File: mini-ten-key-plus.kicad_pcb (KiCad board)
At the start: 2 copper layers, 45 parts, among them SW0 SW_Push, U0 ProMicro

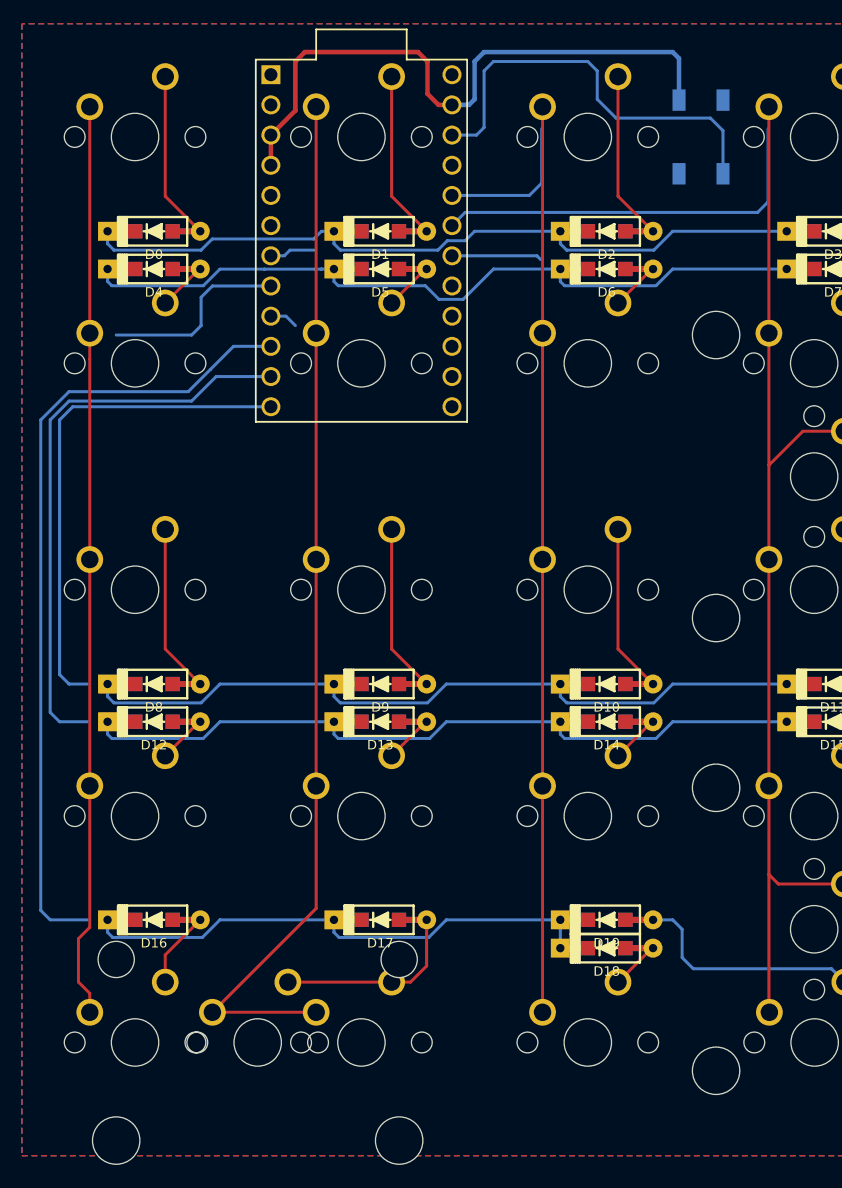
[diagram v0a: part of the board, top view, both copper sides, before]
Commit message: Rotated Pro Micro around
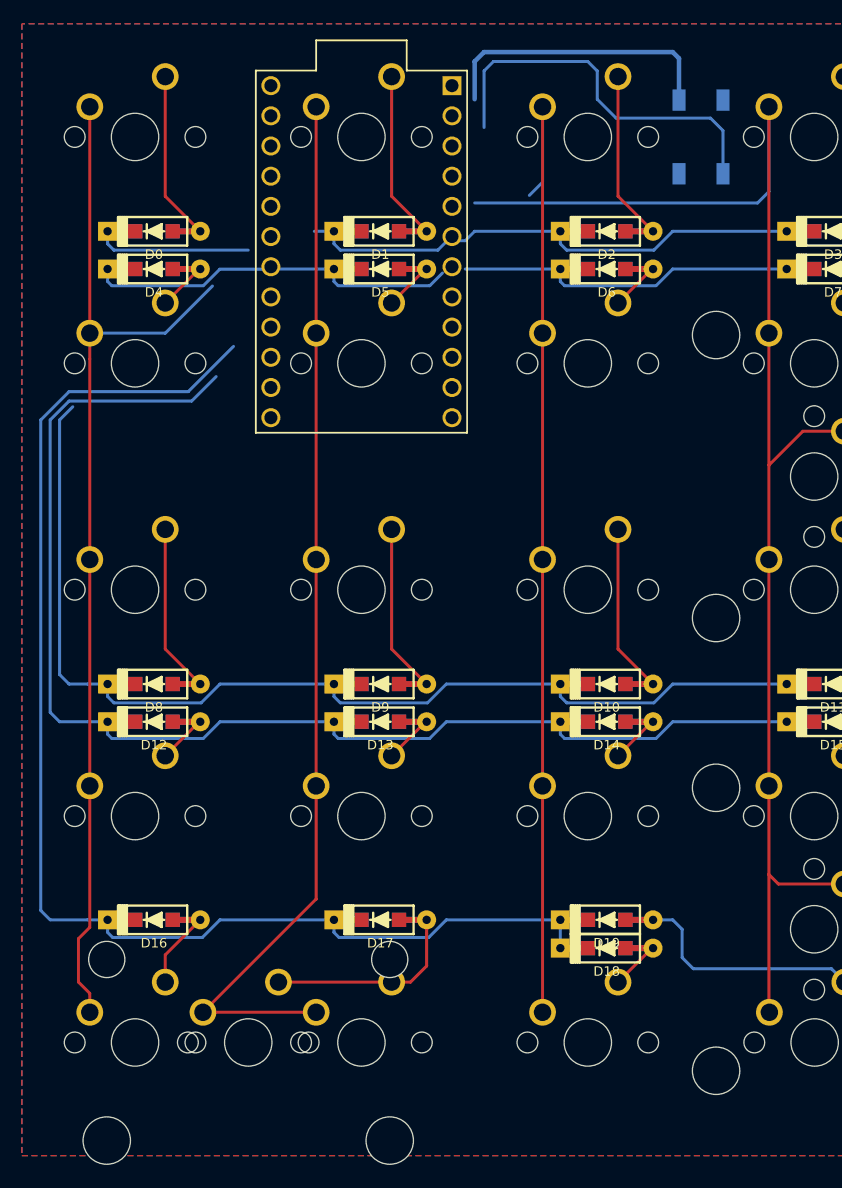
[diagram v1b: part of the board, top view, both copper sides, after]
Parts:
- U0: moved to B.Cu
- moved U0 0.92 mm to (52.4, 50.9)
- moved MX21 0.79 mm to (42.9, 117.5)
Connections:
- U0 pad 10: IO -> ROW4
- U0 pad 11: IO -> ROW3
- U0 pad 12: IO -> ROW2
- U0 pad 17: IO -> Net-(U0-Pad17)
- U0 pad 18: IO -> ROW1
- U0 pad 19: IO -> COL3
- U0 pad 20: IO -> COL2
- U0 pad 7: IO -> ROW0
- U0 pad 8: IO -> COL0
- U0 pad 9: IO -> COL1
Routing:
- net IO: track 234.2 -> 0.00 mm
- net ROW4: track 44.2 -> 110.2 mm
- net ROW3: track 62.5 -> 107.7 mm
- net COL3: track 90.4 -> 122.7 mm
- net GND: track 53.1 -> 24.4 mm
- net ROW2: track 62.9 -> 90.3 mm
- net COL0: track 77.0 -> 89.0 mm
- net COL2: track 76.2 -> 84.1 mm
- net ROW0: track 62.9 -> 56.7 mm
- net ROW1: track 63.4 -> 60.4 mm
- net RESET: track 35.6 -> 32.6 mm
- net COL1: track 88.5 -> 89.7 mm

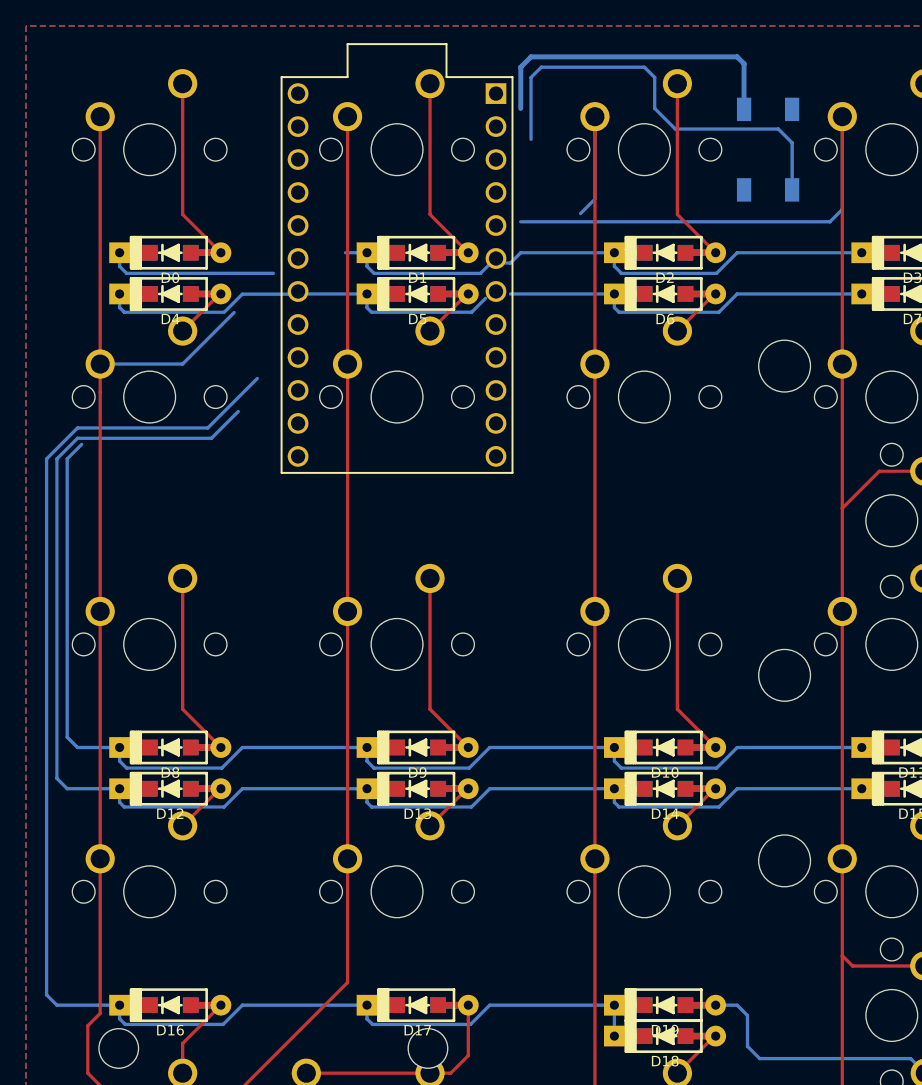
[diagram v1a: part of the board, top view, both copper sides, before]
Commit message: Flipped Pro Micro and redid rows/cols
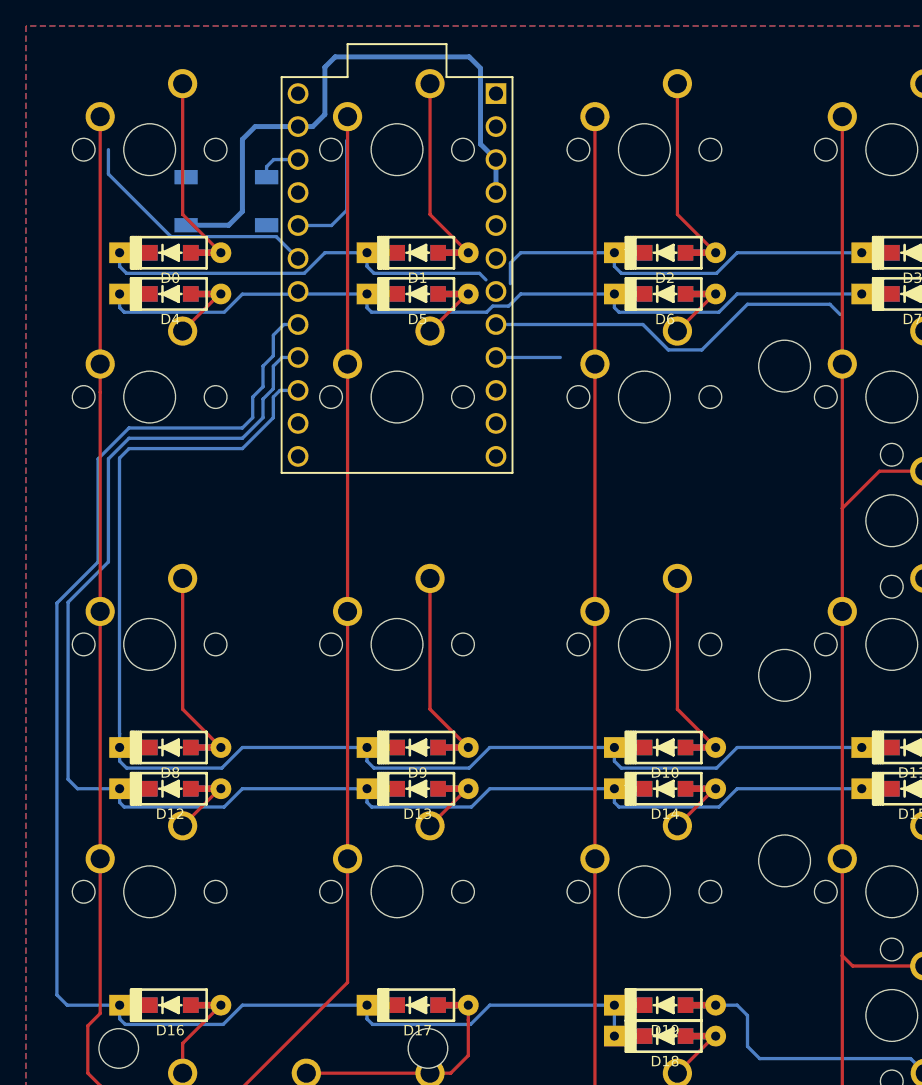
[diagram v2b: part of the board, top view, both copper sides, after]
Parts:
- moved SW0 41.9 mm to (39.2, 45.2), turned to 0 degrees
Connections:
- U0 pad 10: ROW4 -> Net-(U0-Pad10)
- U0 pad 11: ROW3 -> Net-(U0-Pad11)
- U0 pad 12: ROW2 -> Net-(U0-Pad12)
- U0 pad 15: Net-(U0-Pad15) -> ROW2
- U0 pad 16: Net-(U0-Pad16) -> ROW3
- U0 pad 17: Net-(U0-Pad17) -> ROW4
- U0 pad 19: COL3 -> COL0
- U0 pad 20: COL2 -> COL1
- U0 pad 8: COL0 -> COL3
- U0 pad 9: COL1 -> COL2
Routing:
- net RESET: track 32.6 -> 3.46 mm
- net GND: track 24.4 -> 43.9 mm
- net ROW2: track 90.3 -> 102.1 mm
- net COL1: track 89.7 -> 99.3 mm
- net COL0: track 89.0 -> 96.2 mm
- net ROW0: track 56.7 -> 62.5 mm
- net ROW3: track 107.7 -> 112.4 mm
- net ROW4: track 110.2 -> 114.4 mm
- net COL3: track 122.7 -> 119.5 mm
- net COL2: track 84.1 -> 81.2 mm
- net ROW1: track 60.4 -> 62.5 mm

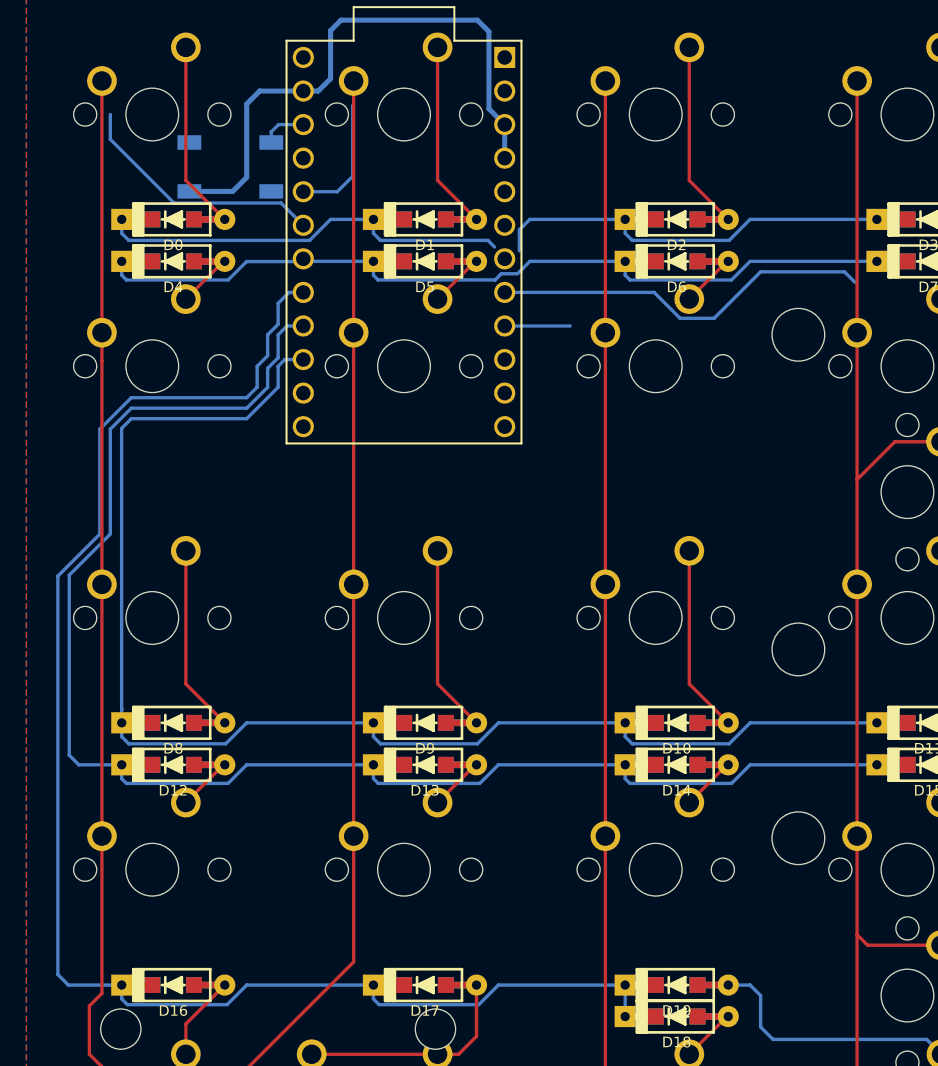
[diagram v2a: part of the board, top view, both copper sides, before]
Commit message: Trying to remove row 4 trace
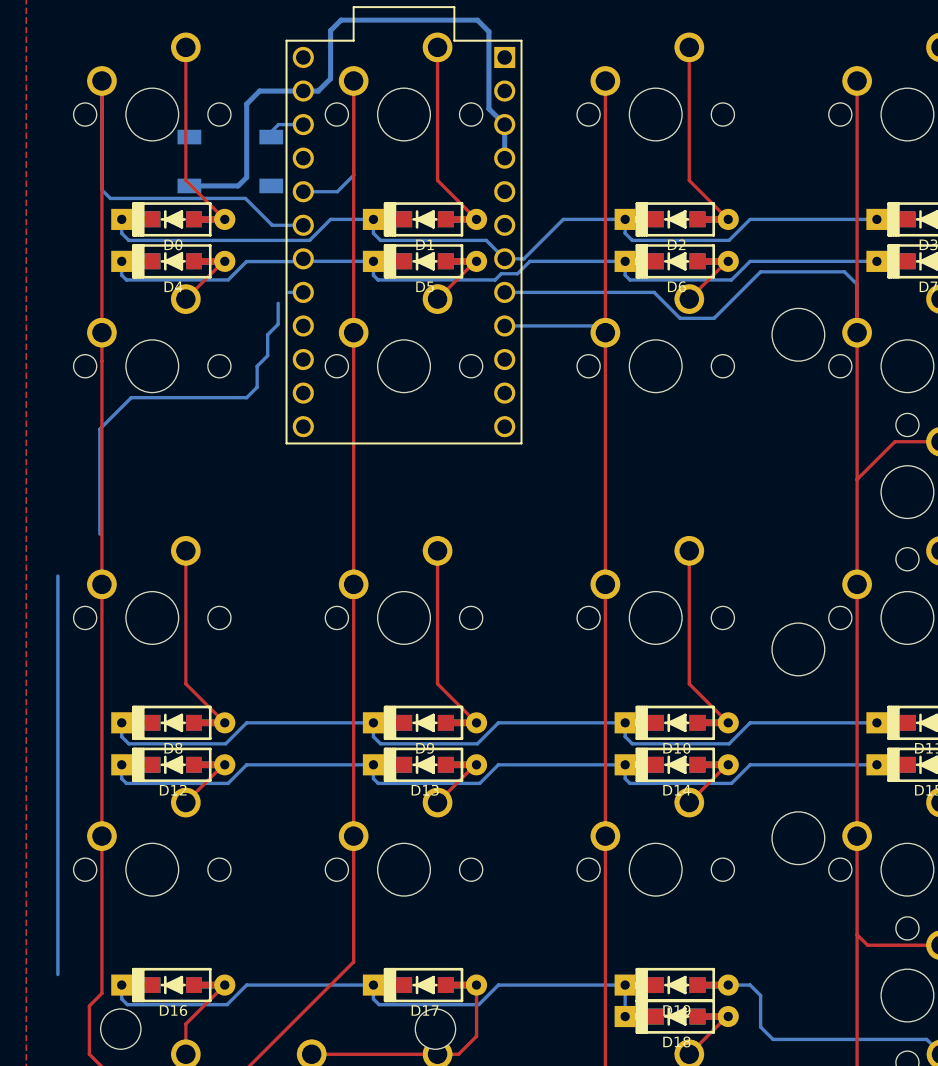
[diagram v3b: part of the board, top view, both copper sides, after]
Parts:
- moved SW0 0.41 mm to (39.2, 44.8)
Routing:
- net ROW3: track 112.4 -> 62.5 mm
- net ROW2: track 102.1 -> 62.9 mm
- net ROW4: track 114.4 -> 103.6 mm
- net COL0: track 96.2 -> 101.6 mm
- net COL3: track 119.5 -> 123.4 mm
- net COL2: track 81.2 -> 84.0 mm
- net COL1: track 99.3 -> 101.1 mm
- net ROW0: track 62.5 -> 64.1 mm

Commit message: General routing
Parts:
- added H0: MountingHole_Pad, mini-general-tweaks:MountingHole_2.2mm_M2_Pad_tweaked, F.Cu at (264.3, 78.6)
- added H1: MountingHole_Pad, mini-general-tweaks:MountingHole_2.2mm_M2_Pad_tweaked, F.Cu at (226.2, 126.2)
- added H2: MountingHole_Pad, mini-general-tweaks:MountingHole_2.2mm_M2_Pad_tweaked, F.Cu at (264.3, 126.2)
- added H3: MountingHole_Pad, mini-general-tweaks:MountingHole_2.2mm_M2_Pad_tweaked, F.Cu at (245.3, 154.8)
- added H4: MountingHole_Pad, mini-general-tweaks:MountingHole_2.2mm_M2_Pad_tweaked, F.Cu at (210.2, 88.1)
- MX21: footprint mini-MX-Tweaks:MXOnly-2U-NoLED_tweak -> mini-MX-Tweaks:MXOnly-2U-NoLED_FLIPPED_tweak
- moved D16 214.3 mm to (245.9, 144.5)
- moved SW0 197.1 mm to (226.2, 107.2)
- moved D17 196.0 mm to (245.9, 146.8)
- moved D10 187.1 mm to (256.4, 124.6)
- moved D13 187.1 mm to (237.3, 127.8)
- moved D14 187.1 mm to (256.4, 127.8)
- moved D18 187.1 mm to (256.4, 146.8)
- moved D19 187.1 mm to (256.4, 144.5)
- moved D2 187.1 mm to (256.4, 86.5)
- moved D6 187.1 mm to (256.4, 89.7)
- moved D9 187.1 mm to (237.3, 124.6)
- moved D0 187.1 mm to (218.3, 86.5)
- moved D11 187.1 mm to (275.4, 124.6)
- moved D12 187.1 mm to (218.3, 127.8)
- moved D15 187.1 mm to (275.4, 127.8)
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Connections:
- U0 pad 10: Net-(U0-Pad10) -> ROW4
- U0 pad 11: Net-(U0-Pad11) -> ROW3
- U0 pad 12: Net-(U0-Pad12) -> ROW2
- U0 pad 15: ROW2 -> Net-(U0-Pad15)
- U0 pad 16: ROW3 -> ROW1
- U0 pad 17: ROW4 -> Net-(U0-Pad17)
- U0 pad 18: ROW1 -> Net-(U0-Pad18)
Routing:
- net ROW3: track 62.5 -> 105.4 mm
- net GND: track 43.7 -> 3.08 mm, vias 0 -> 1
- net ROW2: track 62.9 -> 102.2 mm
- net ROW4: track 103.6 -> 71.2 mm
- net Net-(D16-Pad2): track 6.46 -> 38.4 mm
- net RESET: track 3.46 -> 34.0 mm, vias 0 -> 1
- net COL1: track 101.1 -> 89.7 mm
- net Net-(D17-Pad2): track 16.1 -> 23.1 mm
- net ROW1: track 62.5 -> 67.9 mm
- net COL2: track 84.0 -> 87.3 mm
- net ROW0: track 64.1 -> 66.8 mm
- net COL0: track 101.6 -> 103.4 mm
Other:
- board outline added: 76.2 x 95.3 mm
